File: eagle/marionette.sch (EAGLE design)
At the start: 485 parts, among them J12 IDC_RECEPTACLE_20PIN-S9172-ND, J13 CONN_HEADER_JTAG, J2 SP3T Jumper Switch, J22 ZX62D-B-5P8, J3 IDC_RECEPTACLE_2X20-S9175-ND, J5 CON_COAX_PWR_PJ-047AH-NO_MILL, J8 IDC_RECEPTACLE_2X20-S9175-ND, J9 IDC_RECEPTACLE_2X20-S9175-ND, M5002 IRFR9024NTRPBF, Q1 BSS84, Q2 NFET_DUAL_DMN63D8LDW, SW1 SW-MOM-TACTILE-B3F-1000, SW2 SW-MOM-TACTILE-B3F-1000, U1 SWITCH_74HC4066D, U10 LMV344, U11 STM32F427-STM32F427, U13 CON_HIROSE_DM3D(MICROSD), U14 USB3320, U15 SWITCH_74HC4066D, U17 LM3671, U2 FR014H5JZ, U3 MIC5305_MIC5305-3.3YD5, U4 DAC124S085CIMM, U40 MIC5305_MIC5305-3.3YD5, U41 MIC5305-MIC5305-1.8YD5, U5 MAX3051ESAESA+, U5002 TPS40200, U6 OPAMP_DUAL_MC4558CDT, U7 LMV344, U8 LMV344, U9 LMV344, X1 ABSO7

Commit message: Major library cleanup.  Ran exp-lib.ulp so that all components now point to marionette.lbr or their own particular library (i.e. DAC124S085.lbr) within the marionette_hardware/eagle/ directory.  There are some GND symbols from SUPPLY.lbr and some from GROUND.lbr which I'm ignoring
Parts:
- removed D25: (no value), marionette:DIODE_SCHOTTKY--BAS40-00_SOT23-3
- removed TP29: (no value), marionette:PAD+X-0.7-NO_CREAM+SILK
- D1, D10, D11, D12, D13, D14, D15, D16, D17, D18, D2, D5, D6, D7, D8, D9: device apdm_ap_v2:ESD8006-ESD8006 -> marionette:ESD8006-ESD8006
- D3: value (none) -> BAS40-00
- J1, J10, J11, J6, J7: device monitor-v2:JUMPER-SHORTED-CUTTABLE-E0402-0.3MM -> marionette:JUMPER-SHORTED-CUTTABLE-E0402-0.3MM
- SB1, SB2, SB3: device apdm_dock_testjig:TRACE_BRIDGE_6MIL -> marionette:TRACE_BRIDGE_6MIL
- TP1, TP130, TP132, TP2, TP3, TP35, TP76: device apdm:PAD+X-1.0-NO_CREAM+SILK -> marionette:PAD+X-0.7-NO_CREAM+SILK
- TP10, TP5, TP6, TP7, TP8, TP84, TP9: device dock_v2:PAD+X-2.0-CREAM+SILK -> marionette:PAD+X-1.0-NO_CREAM+SILK
- TP101, TP102, TP105, TP106, TP129, TP139, TP14, TP24, TP25, TP26, TP48, TP50, TP72, TP77, TP79, TP81, TP82, TP83, TP85, TP86, TP89, TP90, TP93, TP94, TP97, TP98: device dock_v2:PAD+X-1.0-NO_CREAM+SILK -> marionette:PAD+X-0.7-NO_CREAM+SILK
- TP11, TP12, TP16, TP17, TP80: device dock_v2:PAD+X-2.0-NOCREAM+SILK -> marionette:PAD+X-1.0-NO_CREAM+SILK
- TP13, TP133, TP134, TP135, TP138, TP140, TP141, TP145, TP200, TP201, TP34, TP36, TP39, TP4, TP40, TP41, TP45, TP49, TP51, TP52, TP53, TP61, TP62, TP73: device dock_v2:PAD+VIA_0.6MM -> marionette:PAD+VIA_0.6MM
- TP137: device dock_v2:PAD+X-2.0-NOCREAM+SILK -> marionette:PAD+X-0.7-NO_CREAM+SILK
- TP18, TP28, TP37, TP38: device dock_v2:PAD+X-0.7-NO_CREAM+SILK -> marionette:PAD+X-0.7-NO_CREAM+SILK
- TP19, TP46, TP47: device marionette:PAD+X-1.0-NO_CREAM+SILK -> marionette:PAD+X-0.7-NO_CREAM+SILK
- TP300, TP301, TP32, TP33: device dock_v2:PAD+VIA_0.25MM -> marionette:PAD+VIA_0.25MM
- TP42, TP43, TP44, TP54, TP55, TP56, TP57, TP58, TP59: device dock_v2:PAD+VIA_GND_0.6MM -> marionette:PAD+VIA_GND_0.6MM
- TP60, TP68, TP69, TP75: device dock_v2:PAD+VIA_GND_0.25MM -> marionette:PAD+VIA_GND_0.25MM
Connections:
- net N$1 renamed VBAT_ANODE
- net OSC_IN: no longer TP29.P
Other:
- note added: "2.0"
- note added: "Headers"
- note added: "POWER"
- note added: "STM32"
- note added: "Snip Jumper and add resistor to add protection to DAC output if necessary."

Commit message: Made some small stylistic changes to the marionette.sch and started work on bom
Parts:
- C101, C102, C103, C112, C113, C114, C99: value 10uF -> 10u
- C110: value 470pF -> 470p
- C152: value 100nF -> 100n
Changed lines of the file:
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@@
 <setting verticaltext="up"/>
 </settings>
-<grid distance="0.05" unitdist="inch" unit="inch" style="lines" multiple="2" display="no" altdistance="0.01" altunitdist="inch" altunit="inch"/>
+<grid distance="0.1" unitdist="inch" unit="inch" style="lines" multiple="1" display="no" altdistance="0.01" altunitdist="inch" altunit="inch"/>
 <layers>
 <layer number="1" name="Top" color="4" fill="1" visible="no" active="no"/>
@@
 <part name="GND51" library="GROUND" deviceset="GND" device=""/>
 <part name="L1" library="marionette" deviceset="INDUCTOR_COUPLED" device="_SRF1260-4R7Y" value="SRF1260-4R7Y"/>
-<part name="C99" library="rcl_custom" deviceset="C-EU" device="C1210" value="10uF">
+<part name="C99" library="rcl_custom" deviceset="C-EU" device="C1210" value="10u">
 <attribute name="V_RATING" value="35V"/>
 </part>
@@
 <attribute name="V_RATING" value="35V"/>
 </part>
-<part name="C101" library="rcl_custom" deviceset="C-EU" device="C1210" value="10uF">
-<attribute name="V_RATING" value="35V"/>
-</part>
-<part name="C102" library="rcl_custom" deviceset="C-EU" device="C1210" value="10uF">
-<attribute name="V_RATING" value="35V"/>
-</part>
-<part name="C103" library="rcl_custom" deviceset="C-EU" device="C1210" value="10uF">
+<part name="C101" library="rcl_custom" deviceset="C-EU" device="C1210" value="10u">
+<attribute name="V_RATING" value="35V"/>
+</part>
+<part name="C102" library="rcl_custom" deviceset="C-EU" device="C1210" value="10u">
+<attribute name="V_RATING" value="35V"/>
+</part>
+<part name="C103" library="rcl_custom" deviceset="C-EU" device="C1210" value="10u">
 <attribute name="V_RATING" value="35V"/>
 </part>
@@
 <part name="R68" library="rcl_custom" deviceset="R-US_" device="0402-B" value="1k"/>
 <part name="R69" library="rcl_custom" deviceset="R-US_" device="0402-B" value="1.6k"/>
-<part name="C110" library="rcl_custom" deviceset="C-EU" device="0402-B" value="470pF">
+<part name="C110" library="rcl_custom" deviceset="C-EU" device="0402-B" value="470p">
 <attribute name="V_RATING" value="25V"/>
 </part>
@@
 <attribute name="V_RATING" value="10V"/>
 </part>
-<part name="C112" library="rcl_custom" deviceset="C-EU" device="C1210" value="10uF">
-<attribute name="V_RATING" value="10V"/>
-</part>
-<part name="C113" library="rcl_custom" deviceset="C-EU" device="C1210" value="10uF">
-<attribute name="V_RATING" value="10V"/>
-</part>
-<part name="C114" library="rcl_custom" deviceset="C-EU" device="C1210" value="10uF">
+<part name="C112" library="rcl_custom" deviceset="C-EU" device="C1210" value="10u">
+<attribute name="V_RATING" value="10V"/>
+</part>
+<part name="C113" library="rcl_custom" deviceset="C-EU" device="C1210" value="10u">
+<attribute name="V_RATING" value="10V"/>
+</part>
+<part name="C114" library="rcl_custom" deviceset="C-EU" device="C1210" value="10u">
 <attribute name="V_RATING" value="10V"/>
 </part>
@@
 <part name="GND98" library="GROUND" deviceset="GND" device=""/>
 <part name="R105" library="rcl_custom" deviceset="R-US_" device="0402-B" value="1k"/>
-<part name="C152" library="rcl_custom" deviceset="C-EU" device="0402-B" value="100nF">
-<attribute name="V_RATING" value="10V"/>
-</part>
+<part name="C152" library="rcl_custom" deviceset="C-EU" device="0402-B" value="100n">
+<attribute name="V_RATING" value="10V"/>
+</part>

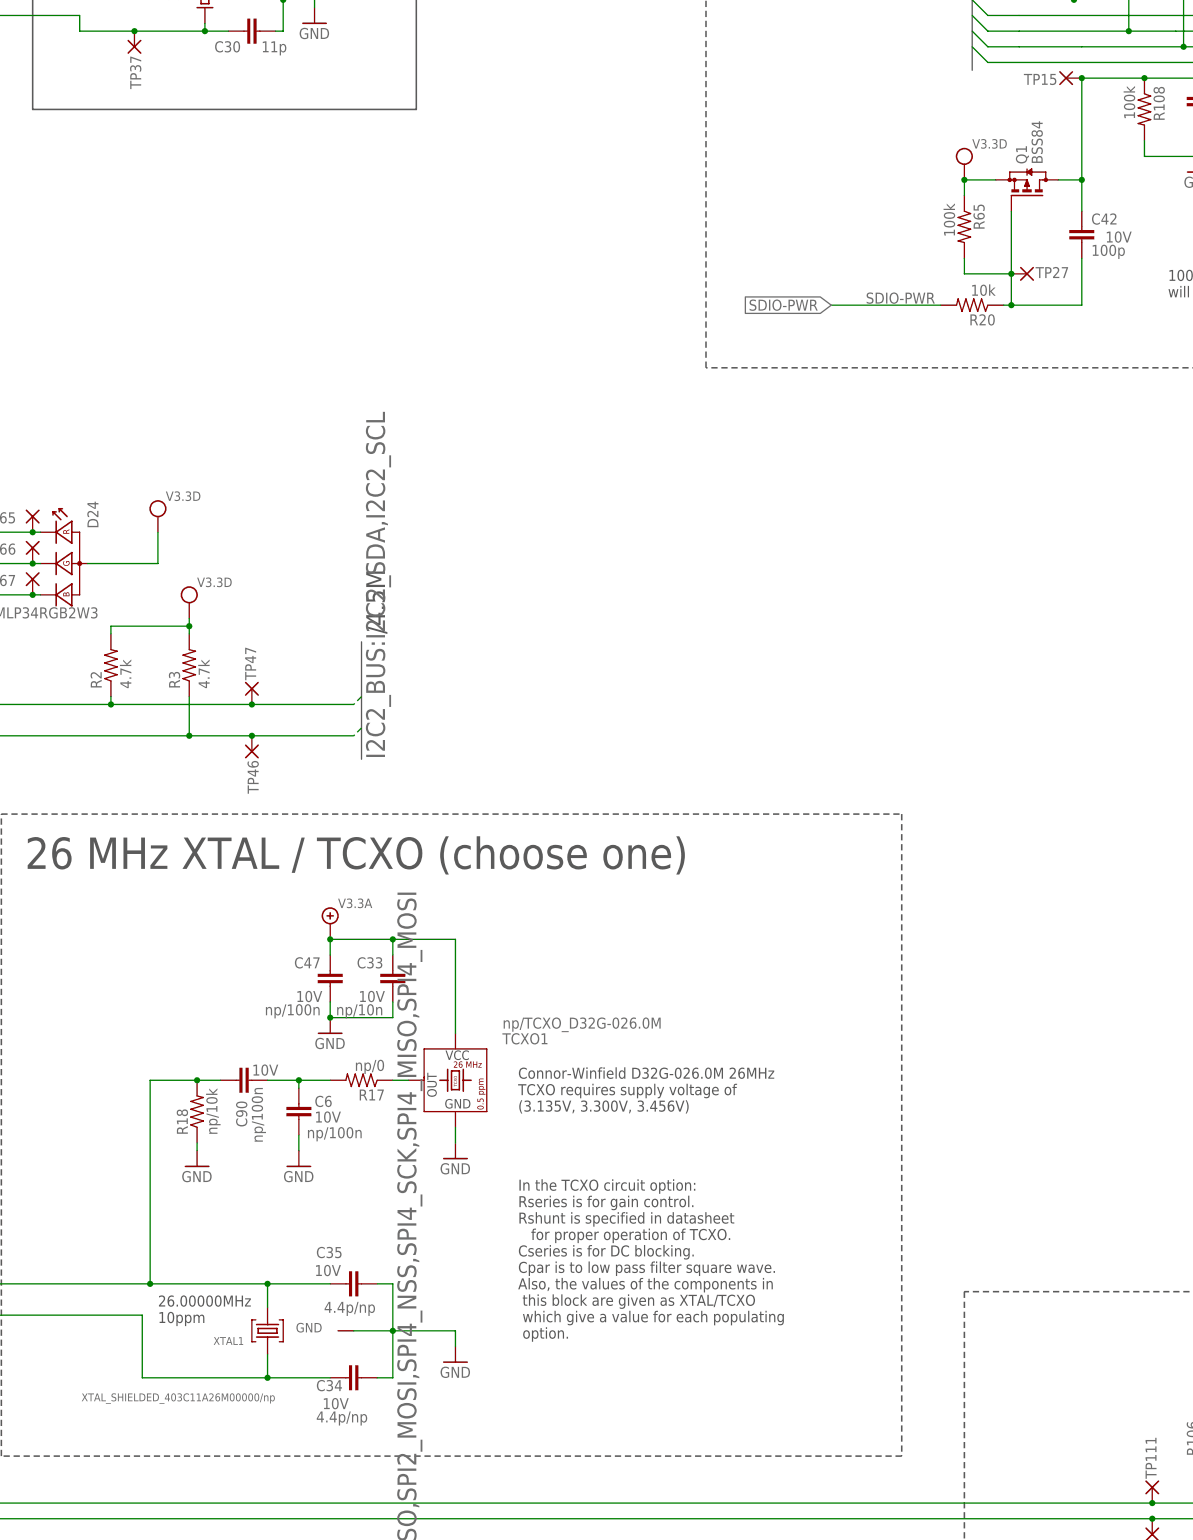
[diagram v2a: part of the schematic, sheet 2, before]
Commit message: Caught some problems with schematic while making BOM.  The MIC5305 in fixed output voltages is not stocked at digikey (or mouser), so had to find some other fixed LDOs to substitute.  Bottom line, never use a fixed LDO if you can help it.
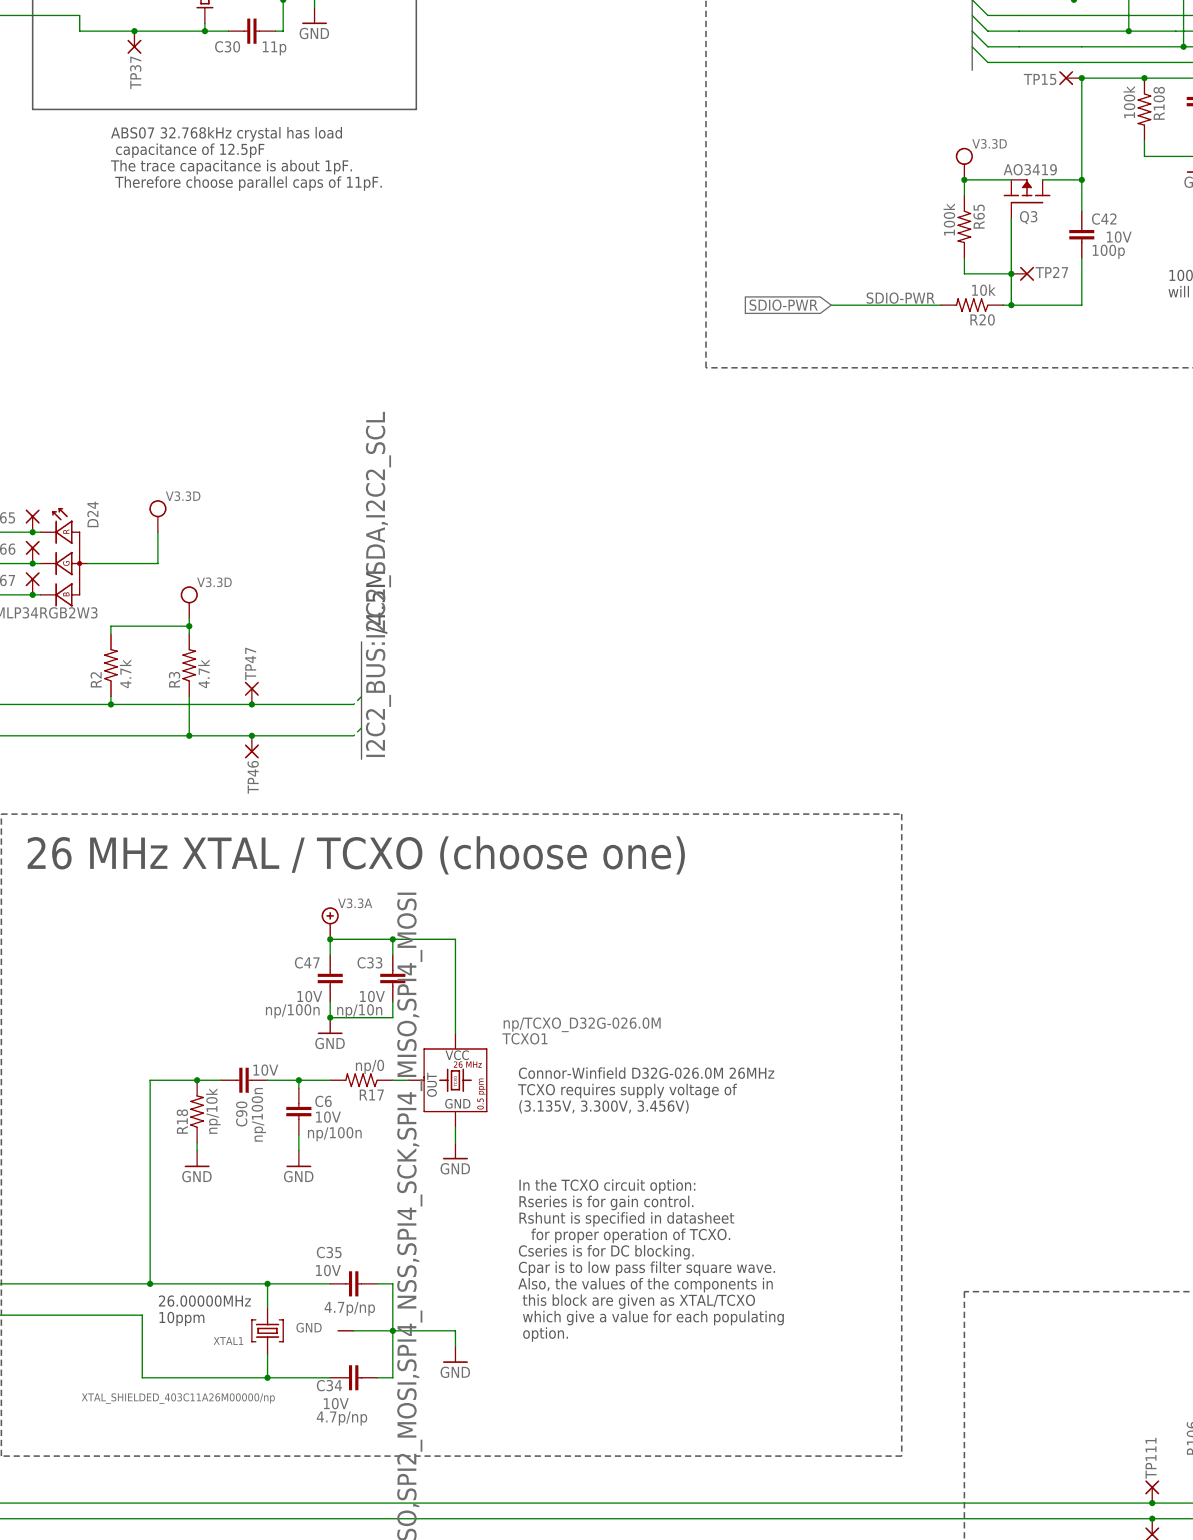
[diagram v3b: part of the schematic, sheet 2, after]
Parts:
- removed Q1: BSS84, BSS84:BSS84
- added Q3: AO3419, apdm_alt:PFET-AO3419
- C110: value 470p -> 1n
- C144: value 220p -> 100p
- C34, C35: value 4.4p/np -> 4.7p/np
- R38: value 86.6k -> 200k
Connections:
- net SDIO-PWR-SWITCHED: now also Q3.D; no longer Q1.D
- net SDIO-PWR_GATE: now also Q3.G; no longer Q1.G
- net V3.3D: now also Q3.S; no longer Q1.S
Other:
- note added: "ABS07 32.768kHz crystal has load capacitance of 12.5pF The trace capacitance is about 1pF. Therefore choose parallel caps of 11pF."
- note added: "MIC5305 fixed regulators are non-stocked at Mouser and Digikey. Also their accuracy is only 1%, so this was stupid choice. Should use adjustable regulators for BOM reduction in future."
- note added: "Temporary fix for V2.0 is using the ADP121 1% LDO from Analog."
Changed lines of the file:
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@@
 <setting verticaltext="up"/>
 </settings>
-<grid distance="0.1" unitdist="inch" unit="inch" style="lines" multiple="1" display="no" altdistance="0.01" altunitdist="inch" altunit="inch"/>
+<grid distance="0.05" unitdist="inch" unit="inch" style="lines" multiple="2" display="no" altdistance="0.01" altunitdist="inch" altunit="inch"/>
 <layers>
 <layer number="1" name="Top" color="4" fill="1" visible="no" active="no"/>
@@
 <part name="D3" library="marionette" deviceset="DIODE_SCHOTTKY-*" device="-BAS40-00_SOT23-3" value="BAS40-00"/>
 <part name="R19" library="rcl_custom" deviceset="R-US_" device="0402-B" value="1k"/>
-<part name="C34" library="rcl_custom" deviceset="C-EU" device="0402-B" value="4.4p/np">
+<part name="C34" library="rcl_custom" deviceset="C-EU" device="0402-B" value="4.7p/np">
 <attribute name="V_RATING" value="10V"/>
 </part>
-<part name="C35" library="rcl_custom" deviceset="C-EU" device="0402-B" value="4.4p/np">
+<part name="C35" library="rcl_custom" deviceset="C-EU" device="0402-B" value="4.7p/np">
 <attribute name="V_RATING" value="10V"/>
 </part>
@@
 <part name="GND16" library="GROUND" deviceset="GND" device=""/>
 <part name="GND26" library="GROUND" deviceset="GND" device=""/>
-<part name="Q1" library="BSS84" deviceset="BSS84" device=""/>
 <part name="C42" library="rcl_custom" deviceset="C-EU" device="0402-B" value="100p">
 <attribute name="V_RATING" value="10V"/>
@@
 <attribute name="V_RATING" value="25V"/>
 </part>
-<part name="R38" library="rcl_custom" deviceset="R-US_" device="0402-B" value="86.6k"/>
+<part name="R38" library="rcl_custom" deviceset="R-US_" device="0402-B" value="200k"/>
 <part name="R68" library="rcl_custom" deviceset="R-US_" device="0402-B" value="1k"/>
 <part name="R69" library="rcl_custom" deviceset="R-US_" device="0402-B" value="1.6k"/>
-<part name="C110" library="rcl_custom" deviceset="C-EU" device="0402-B" value="470p">
+<part name="C110" library="rcl_custom" deviceset="C-EU" device="0402-B" value="1n">
 <attribute name="V_RATING" value="25V"/>
 </part>
@@
 <part name="R97" library="rcl_custom" deviceset="R-US_" device="0402-B" value="15k"/>
 <part name="R98" library="rcl_custom" deviceset="R-US_" device="0402-B" value="np"/>
-<part name="C144" library="rcl_custom" deviceset="C-EU" device="0402-B" value="220p">
+<part name="C144" library="rcl_custom" deviceset="C-EU" device="0402-B" value="100p">
 <attribute name="V_RATING" value="50V"/>
 </part>
@@
 <attribute name="V_RATING" value="35V"/>
 </part>
+<part name="Q3" library="apdm_alt" deviceset="PFET" device="-AO3419" value="AO3419"/>
 </parts>
 <sheets>
@@
 <text x="1101.09" y="5.08" size="5.08" layer="94">2.0</text>
 <text x="1026.16" y="24.13" size="7.62" layer="94">POWER</text>
+<text x="861.06" y="276.86" size="7.62" layer="112">MIC5305 fixed regulators are non-stocked at Mouser and Digikey.  Also their accuracy is only 1%, so this was stupid choice.  Should use adjustable regulators for BOM reduction in future.</text>
+<text x="862.33" y="261.62" size="7.62" layer="112">Temporary fix for V2.0 is using the ADP121 1% LDO from Analog.</text>
 </plain>
 <instances>
@@
 <text x="1099.82" y="5.08" size="5.08" layer="94">2.0</text>
 <text x="1027.43" y="25.4" size="7.62" layer="94">STM32</text>
+<text x="213.36" y="543.56" size="1.778" layer="97">ABS07 32.768kHz crystal has load
+ capacitance of 12.5pF
+The trace capacitance is about 1pF.
+ Therefore choose parallel caps of 11pF.</text>
 </plain>
 <instances>
@@
 <instance part="GND15" gate="1" x="651.51" y="782.32"/>
 <instance part="GND16" gate="1" x="435.61" y="580.39"/>
-<instance part="Q1" gate="G1" x="361.95" y="544.83" rot="R90"/>
 <instance part="C42" gate="CE" x="370.84" y="537.21" smashed="yes">
 <attribute name="V_RATING" x="374.65" y="534.67" size="1.778" layer="96"/>
@@
 <attribute name="VALUE" x="855.98" y="566.42" size="1.778" layer="96"/>
 </instance>
+<instance part="Q3" gate="Q" x="361.95" y="542.29" smashed="yes" rot="MR90">
+<attribute name="VALUE" x="358.14" y="547.37" size="1.778" layer="96" rot="MR180"/>
+<attribute name="NAME" x="360.68" y="539.75" size="1.778" layer="95" rot="MR180"/>
+</instance>
 </instances>
 <busses>
@@
 <net name="SDIO-PWR-SWITCHED" class="0">
 <segment>
-<pinref part="Q1" gate="G1" pin="D"/>
-<wire x1="367.03" y1="544.83" x2="370.84" y2="544.83" width="0.1524" layer="91"/>
+<wire x1="364.49" y1="544.83" x2="370.84" y2="544.83" width="0.1524" layer="91"/>
 <wire x1="370.84" y1="544.83" x2="370.84" y2="561.34" width="0.1524" layer="91"/>
 <wire x1="370.84" y1="561.34" x2="381" y2="561.34" width="0.1524" layer="91"/>
@@
 <pinref part="R108" gate="R" pin="1"/>
 <junction x="381" y="561.34"/>
+<pinref part="Q3" gate="Q" pin="D"/>
 </segment>
 </net>
@@
 <wire x1="351.79" y1="532.13" x2="351.79" y2="529.59" width="0.1524" layer="91"/>
 <wire x1="351.79" y1="529.59" x2="359.41" y2="529.59" width="0.1524" layer="91"/>
-<pinref part="Q1" gate="G1" pin="G"/>
-<wire x1="359.41" y1="529.59" x2="359.41" y2="539.75" width="0.1524" layer="91"/>
+<wire x1="359.41" y1="529.59" x2="359.41" y2="538.48" width="0.1524" layer="91"/>
 <wire x1="370.84" y1="524.51" x2="359.41" y2="524.51" width="0.1524" layer="91"/>
 <wire x1="359.41" y1="524.51" x2="359.41" y2="529.59" width="0.1524" layer="91"/>
@@
 <wire x1="370.84" y1="524.51" x2="370.84" y2="532.13" width="0.1524" layer="91"/>
 <pinref part="TP27" gate="TP" pin="P"/>
+<pinref part="Q3" gate="Q" pin="G"/>
 </segment>
 </net>
@@
 </segment>
 <segment>
-<pinref part="Q1" gate="G1" pin="S"/>
-<wire x1="356.87" y1="544.83" x2="351.79" y2="544.83" width="0.1524" layer="91"/>
+<wire x1="359.41" y1="544.83" x2="351.79" y2="544.83" width="0.1524" layer="91"/>
 <wire x1="351.79" y1="544.83" x2="351.79" y2="542.29" width="0.1524" layer="91"/>
 <pinref part="R65" gate="R" pin="1"/>
 <pinref part="V20" gate="G1" pin="V3.3D"/>
 <junction x="351.79" y="544.83"/>
+<pinref part="Q3" gate="Q" pin="S"/>
 </segment>
 <segment>
